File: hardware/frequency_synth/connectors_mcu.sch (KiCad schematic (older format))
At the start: 14 parts, among them P1001 CONN_01X02, U1001 boosterpack_ti, U1002 CONN_SMA_2GND, U1003 ADM7150

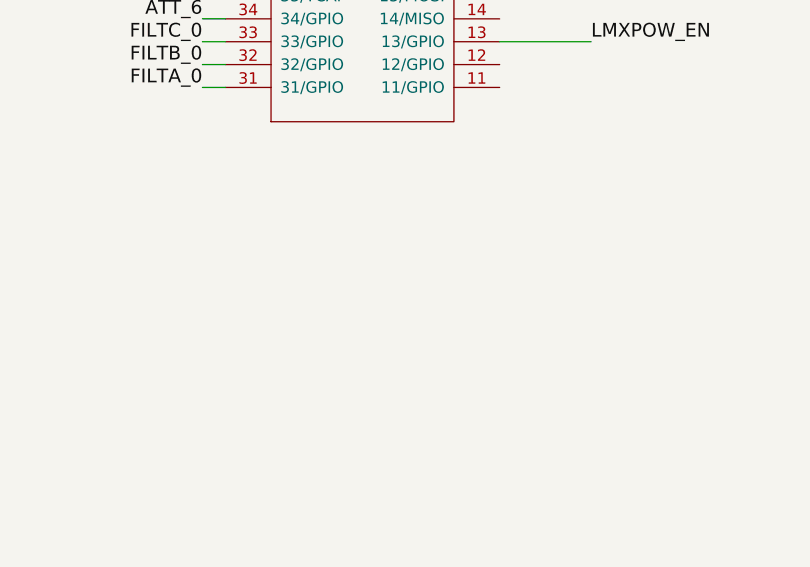
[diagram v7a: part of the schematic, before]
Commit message: work on layout of synth, done up to output stage of lmx2592
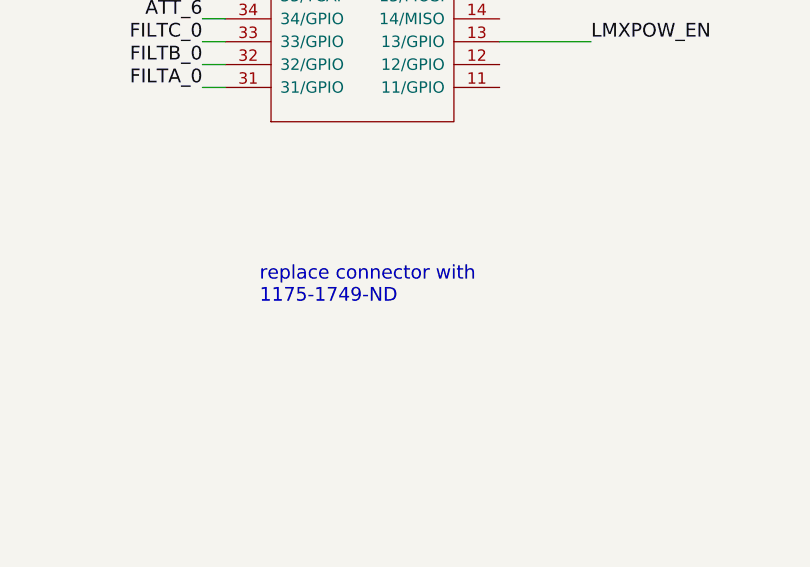
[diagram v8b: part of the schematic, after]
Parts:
- U1001: footprint Connect:IDC_Header_Straight_40pins -> vna_footprints:3221-40-0100-00_conn40
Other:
- note added: "replace connector with\n1175-1749-ND\n"
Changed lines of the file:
@@
 F 0 "U1001" H 1700 4450 60  0000 C CNN
 F 1 "boosterpack_ti" H 1950 4250 60  0000 C CNN
-F 2 "Connect:IDC_Header_Straight_40pins" H 1700 4450 60  0001 C CNN
+F 2 "vna_footprints:3221-40-0100-00_conn40" H 1700 4450 60  0001 C CNN
 F 3 "" H 1700 4450 60  0000 C CNN
 	1    1950 2850
@@
 $EndComp
 $Comp
-L GND #PWR0201
+L GND #PWR0195
 U 1 1 572E0EDA
 P 2650 2950
-F 0 "#PWR0201" H 2650 2700 50  0001 C CNN
+F 0 "#PWR0195" H 2650 2700 50  0001 C CNN
 F 1 "GND" H 2650 2800 50  0000 C CNN
 F 2 "" H 2650 2950 50  0000 C CNN
@@
 $EndComp
 $Comp
-L GND #PWR0202
+L GND #PWR0196
 U 1 1 572E0EDB
 P 2700 1850
-F 0 "#PWR0202" H 2700 1600 50  0001 C CNN
+F 0 "#PWR0196" H 2700 1600 50  0001 C CNN
 F 1 "GND" H 2700 1700 50  0000 C CNN
 F 2 "" H 2700 1850 50  0000 C CNN
@@
 FILTC_0
 $Comp
-L GND #PWR0203
+L GND #PWR0197
 U 1 1 572E0EEC
 P 9800 1200
-F 0 "#PWR0203" H 9800 950 50  0001 C CNN
+F 0 "#PWR0197" H 9800 950 50  0001 C CNN
 F 1 "GND" H 9800 1050 50  0000 C CNN
 F 2 "" H 9800 1200 50  0000 C CNN
@@
 $EndComp
 $Comp
-L +5V #PWR0204
+L +5V #PWR0198
 U 1 1 572E0EEE
 P 9850 1300
-F 0 "#PWR0204" H 9850 1150 50  0001 C CNN
+F 0 "#PWR0198" H 9850 1150 50  0001 C CNN
 F 1 "+5V" H 9850 1440 50  0000 C CNN
 F 2 "" H 9850 1300 50  0000 C CNN
@@
 $EndComp
 $Comp
-L GND #PWR0205
+L GND #PWR0199
 U 1 1 572E0F12
 P 5300 1700
-F 0 "#PWR0205" H 5300 1450 50  0001 C CNN
+F 0 "#PWR0199" H 5300 1450 50  0001 C CNN
 F 1 "GND" H 5300 1550 50  0000 C CNN
 F 2 "" H 5300 1700 50  0000 C CNN
@@
 POWERDET
 $Comp
-L GND #PWR0206
+L GND #PWR0200
 U 1 1 572E0F14
 P 9700 6250
-F 0 "#PWR0206" H 9700 6000 50  0001 C CNN
+F 0 "#PWR0200" H 9700 6000 50  0001 C CNN
 F 1 "GND" H 9700 6100 50  0000 C CNN
 F 2 "" H 9700 6250 50  0000 C CNN
@@
 3V3
 $Comp
-L +3V3 #PWR0207
+L +3V3 #PWR0201
 U 1 1 5730B3CA
 P 9850 1400
-F 0 "#PWR0207" H 9850 1250 50  0001 C CNN
+F 0 "#PWR0201" H 9850 1250 50  0001 C CNN
 F 1 "+3V3" H 9850 1540 50  0000 C CNN
 F 2 "" H 9850 1400 50  0000 C CNN
@@
 $EndComp
 $Comp
-L GND #PWR0208
+L GND #PWR0202
 U 1 1 57328303
 P 6050 2800
-F 0 "#PWR0208" H 6050 2550 50  0001 C CNN
+F 0 "#PWR0202" H 6050 2550 50  0001 C CNN
 F 1 "GND" H 6050 2650 50  0000 C CNN
 F 2 "" H 6050 2800 50  0000 C CNN
@@
 $EndComp
 $Comp
-L +5V #PWR0209
+L +5V #PWR0203
 U 1 1 57328345
 P 6550 1950
-F 0 "#PWR0209" H 6550 1800 50  0001 C CNN
+F 0 "#PWR0203" H 6550 1800 50  0001 C CNN
 F 1 "+5V" H 6550 2090 50  0000 C CNN
 F 2 "" H 6550 1950 50  0000 C CNN
@@
 $EndComp
 $Comp
-L +5V #PWR0210
+L +5V #PWR0204
 U 1 1 572C5D1D
 P 5300 800
-F 0 "#PWR0210" H 5300 650 50  0001 C CNN
+F 0 "#PWR0204" H 5300 650 50  0001 C CNN
 F 1 "+5V" H 5300 940 50  0000 C CNN
 F 2 "" H 5300 800 50  0000 C CNN
@@
 $EndComp
 $Comp
-L GND #PWR0211
+L GND #PWR0205
 U 1 1 572C5E63
 P 4850 1700
-F 0 "#PWR0211" H 4850 1450 50  0001 C CNN
+F 0 "#PWR0205" H 4850 1450 50  0001 C CNN
 F 1 "GND" H 4850 1550 50  0000 C CNN
 F 2 "" H 4850 1700 50  0000 C CNN
@@
 $EndComp
 $Comp
-L +3V3 #PWR0212
+L +3V3 #PWR0206
 U 1 1 572C5EF3
 P 4850 800
-F 0 "#PWR0212" H 4850 650 50  0001 C CNN
+F 0 "#PWR0206" H 4850 650 50  0001 C CNN
 F 1 "+3V3" H 4850 940 50  0000 C CNN
 F 2 "" H 4850 800 50  0000 C CNN
@@
 $EndComp
 $Comp
-L +5V #PWR0213
+L +5V #PWR0207
 U 1 1 572C8470
 P 7600 4600
-F 0 "#PWR0213" H 7600 4450 50  0001 C CNN
+F 0 "#PWR0207" H 7600 4450 50  0001 C CNN
 F 1 "+5V" H 7600 4740 50  0000 C CNN
 F 2 "" H 7600 4600 50  0000 C CNN
@@
 $EndComp
 $Comp
-L +3V3 #PWR0214
+L +3V3 #PWR0208
 U 1 1 572C8526
 P 9950 4500
-F 0 "#PWR0214" H 9950 4350 50  0001 C CNN
+F 0 "#PWR0208" H 9950 4350 50  0001 C CNN
 F 1 "+3V3" H 9950 4640 50  0000 C CNN
 F 2 "" H 9950 4500 50  0000 C CNN
@@
 $EndComp
 $Comp
-L GND #PWR0215
+L GND #PWR0209
 U 1 1 572C88F0
 P 8900 5000
-F 0 "#PWR0215" H 8900 4750 50  0001 C CNN
+F 0 "#PWR0209" H 8900 4750 50  0001 C CNN
 F 1 "GND" H 8900 4850 50  0000 C CNN
 F 2 "" H 8900 5000 50  0000 C CNN
@@
 $EndComp
 $Comp
-L GND #PWR0216
+L GND #PWR0210
 U 1 1 572C8AB5
 P 9800 4400
-F 0 "#PWR0216" H 9800 4150 50  0001 C CNN
+F 0 "#PWR0210" H 9800 4150 50  0001 C CNN
 F 1 "GND" H 9800 4250 50  0000 C CNN
 F 2 "" H 9800 4400 50  0000 C CNN
@@
 $EndComp
 $Comp
-L GND #PWR0217
+L GND #PWR0211
 U 1 1 572C8B7A
 P 9450 4300
-F 0 "#PWR0217" H 9450 4050 50  0001 C CNN
+F 0 "#PWR0211" H 9450 4050 50  0001 C CNN
 F 1 "GND" H 9450 4150 50  0000 C CNN
 F 2 "" H 9450 4300 50  0000 C CNN
@@
 $EndComp
 $Comp
-L GND #PWR0218
+L GND #PWR0212
 U 1 1 572C8D9E
 P 8200 4250
-F 0 "#PWR0218" H 8200 4000 50  0001 C CNN
+F 0 "#PWR0212" H 8200 4000 50  0001 C CNN
 F 1 "GND" H 8200 4100 50  0000 C CNN
 F 2 "" H 8200 4250 50  0000 C CNN
@@
 $EndComp
 $Comp
-L GND #PWR0219
+L GND #PWR0213
 U 1 1 572C910A
 P 8050 5050
-F 0 "#PWR0219" H 8050 4800 50  0001 C CNN
+F 0 "#PWR0213" H 8050 4800 50  0001 C CNN
 F 1 "GND" H 8050 4900 50  0000 C CNN
 F 2 "" H 8050 5050 50  0000 C CNN
@@
 $EndComp
 $Comp
-L GND #PWR0220
+L GND #PWR0214
 U 1 1 572C9289
 P 9700 5050
-F 0 "#PWR0220" H 9700 4800 50  0001 C CNN
+F 0 "#PWR0214" H 9700 4800 50  0001 C CNN
 F 1 "GND" H 9700 4900 50  0000 C CNN
 F 2 "" H 9700 5050 50  0000 C CNN
@@
 $EndComp
 $Comp
-L GND #PWR0221
+L GND #PWR0215
 U 1 1 572C941F
 P 9900 5050
-F 0 "#PWR0221" H 9900 4800 50  0001 C CNN
+F 0 "#PWR0215" H 9900 4800 50  0001 C CNN
 F 1 "GND" H 9900 4900 50  0000 C CNN
 F 2 "" H 9900 5050 50  0000 C CNN
@@
 Wire Wire Line
 	2550 3250 2750 3250
+Text Notes 1500 4800 0    60   ~ 0
+replace connector with\n1175-1749-ND\n
 $EndSCHEMATC
